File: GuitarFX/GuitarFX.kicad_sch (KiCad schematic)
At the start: 0 parts

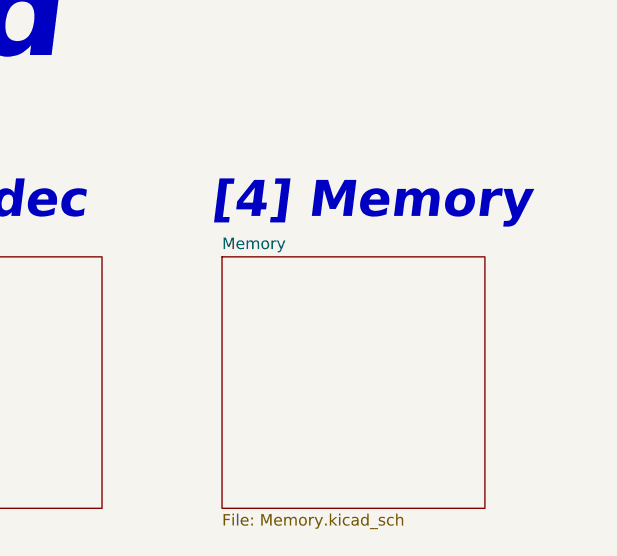
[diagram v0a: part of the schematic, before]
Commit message: Added connections to CODEC
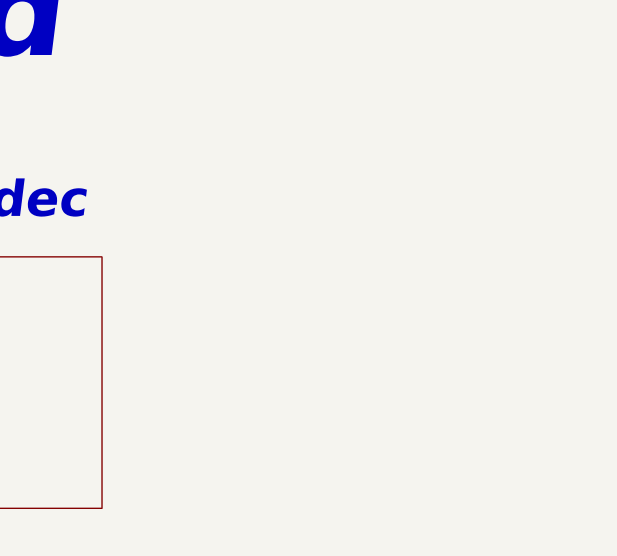
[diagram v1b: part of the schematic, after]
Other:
- removed sheet Memory
- note removed: "[4] Memory"
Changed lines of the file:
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@@
-    (effects (font (size 4 4) (thickness 2) bold italic) (justify left bottom))
-  )
-  (text "[4] Memory" (at 158.75 52.07 0)
     (effects (font (size 4 4) (thickness 2) bold italic) (justify left bottom))
   )
@@
       )
     )
-  )
-  (sheet (at 160.02 55.88) (size 29.21 27.94) (fields_autoplaced)
-    (stroke (width 0.1524) (type solid))
-    (fill (color 0 0 0 0.0000))
-    (property "Sheetname" "Memory" (at 160.02 55.1684 0)
-      (effects (font (size 1.27 1.27)) (justify left bottom))
-    )
-    (property "Sheetfile" "Memory.kicad_sch" (at 160.02 84.4046 0)
-      (effects (font (size 1.27 1.27)) (justify left top))
-    )
-    (instances
-      (project "GuitarFX"
-        (path "/4ab4bfc6-98ca-4cb1-8273-436b96035b51" (page "5"))
-      )
-    )

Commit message: Added decuopling capacitors and filtering to MCU
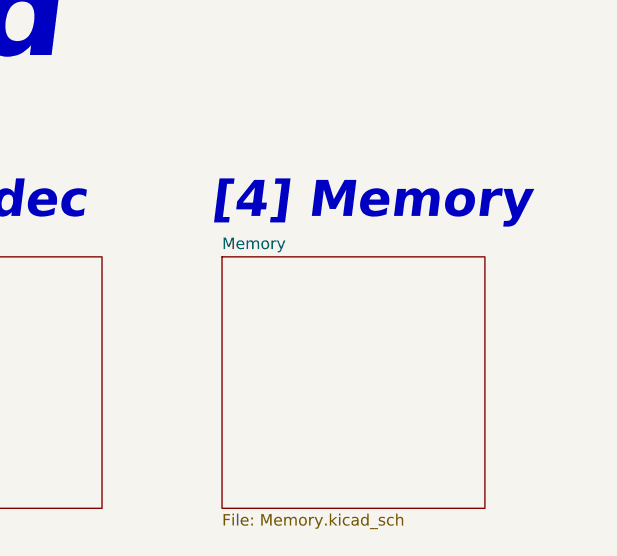
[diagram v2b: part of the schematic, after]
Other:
- added sheet Memory (Memory.kicad_sch)
- note added: "[4] Memory"
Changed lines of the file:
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@@
+    (effects (font (size 4 4) (thickness 2) bold italic) (justify left bottom))
+  )
+  (text "[4] Memory" (at 158.75 52.07 0)
     (effects (font (size 4 4) (thickness 2) bold italic) (justify left bottom))
   )
@@
       )
     )
+  )
+  (sheet (at 160.02 55.88) (size 29.21 27.94) (fields_autoplaced)
+    (stroke (width 0.1524) (type solid))
+    (fill (color 0 0 0 0.0000))
+    (property "Sheetname" "Memory" (at 160.02 55.1684 0)
+      (effects (font (size 1.27 1.27)) (justify left bottom))
+    )
+    (property "Sheetfile" "Memory.kicad_sch" (at 160.02 84.4046 0)
+      (effects (font (size 1.27 1.27)) (justify left top))
+    )
+    (instances
+      (project "GuitarFX"
+        (path "/4ab4bfc6-98ca-4cb1-8273-436b96035b51" (page "5"))
+      )
+    )
